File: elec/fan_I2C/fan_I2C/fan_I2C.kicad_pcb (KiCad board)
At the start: 2 copper layers, 83 x 160 mm, 59 parts, among them J101 DB25_Female_MountingHoles, J102 DB9_Female_MountingHoles, J201 0.100_2Pin, J202 S04B-XASK-1(LF)(SN), J301 RJ12_6P6C_HORZ, J302 0.100_2Pin, Q201 BSS138, Q202 BSS138, Q301 BSS138, Q302 BSS138, Q303 BSS138, Q304 BSS138, SW101 SW_DIP_x08

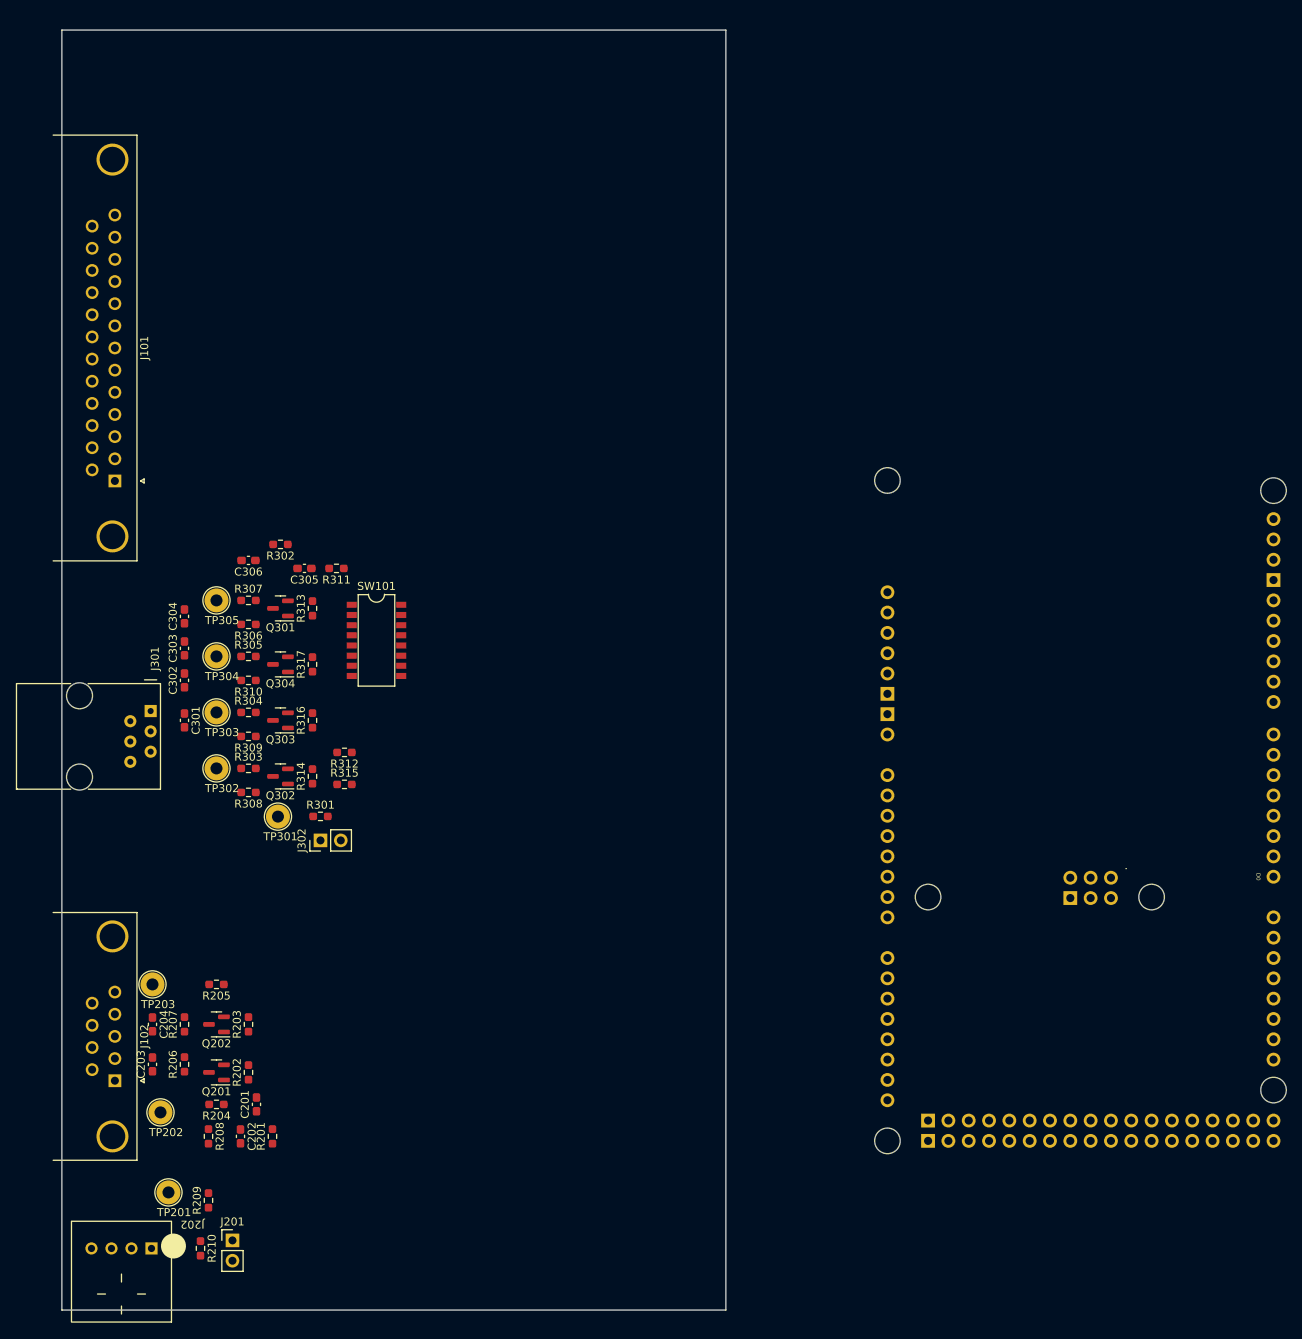
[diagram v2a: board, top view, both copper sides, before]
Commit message: Add connect Due 3V3, 5V and gnd.
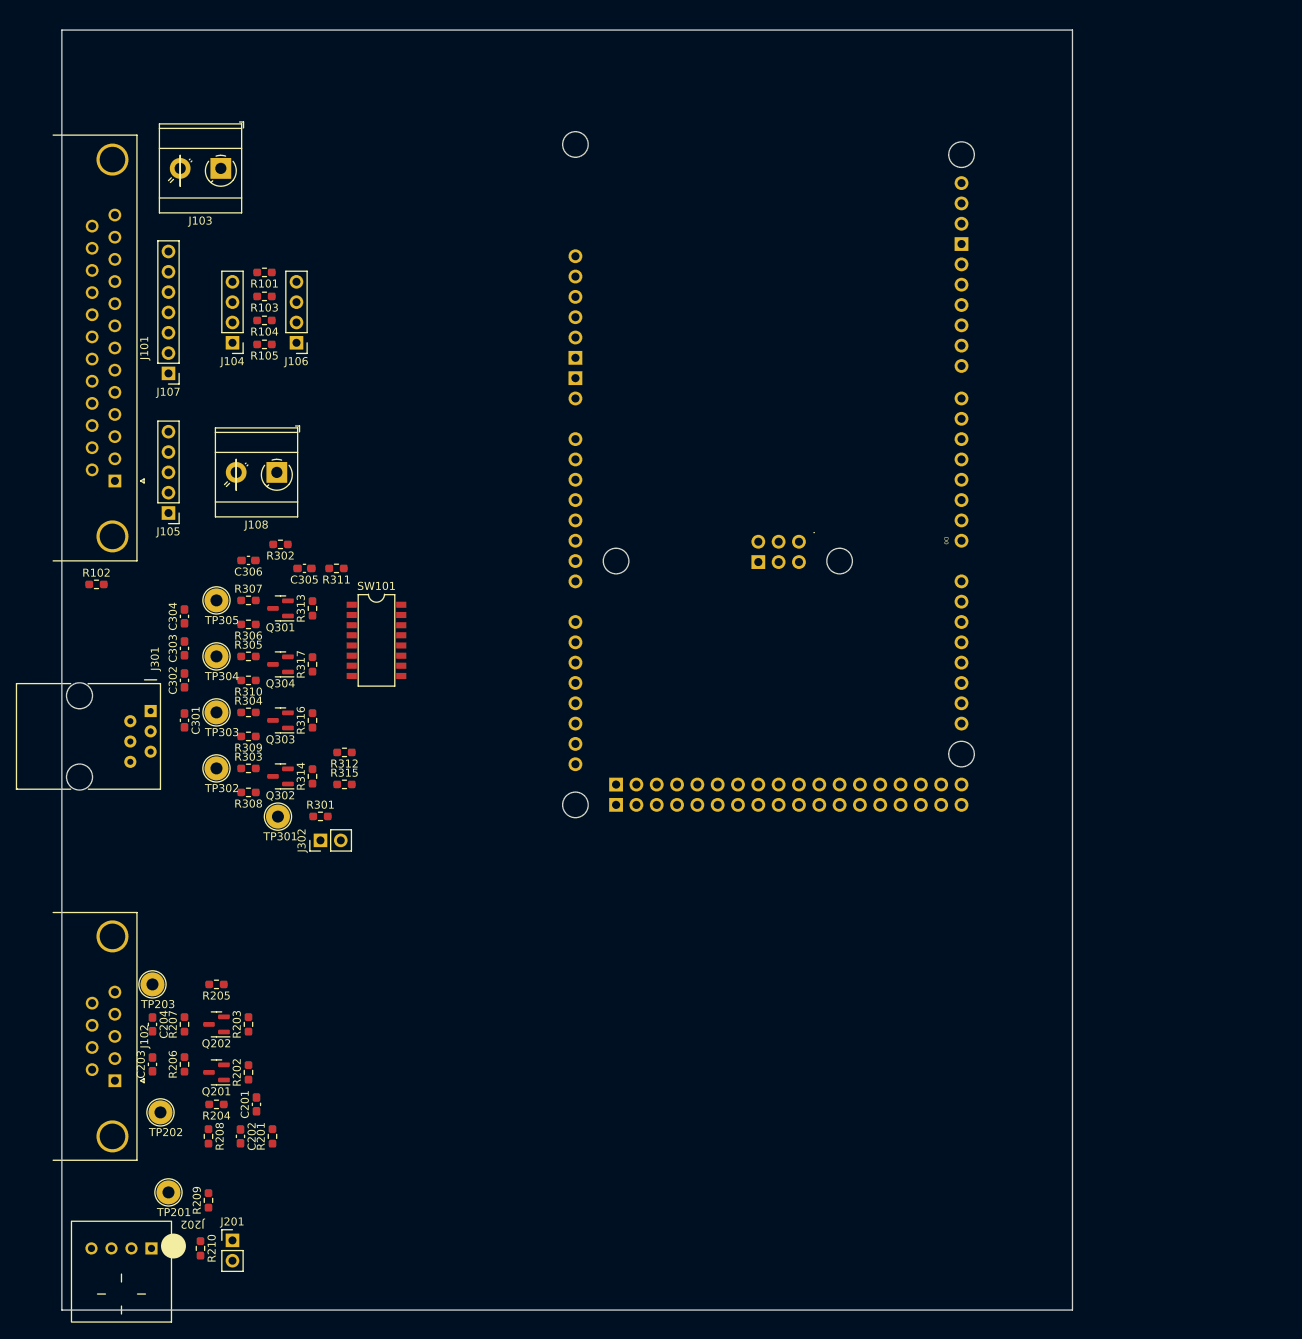
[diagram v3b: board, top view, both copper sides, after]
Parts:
- added J103: Screw_Terminal_01x02, TerminalBlock_MetzConnect:TerminalBlock_MetzConnect_Type073_RT02602HBLU_1x02_P5.08mm_Horizontal, F.Cu at (53.5, 39.0)
- added J104: Conn_01x04, Connector_PinHeader_2.54mm:PinHeader_1x04_P2.54mm_Vertical, F.Cu at (55.0, 60.8)
- added J105: Conn_01x05, Connector_PinHeader_2.54mm:PinHeader_1x05_P2.54mm_Vertical, F.Cu at (47.0, 82.1)
- added J106: Conn_01x04, Connector_PinHeader_2.54mm:PinHeader_1x04_P2.54mm_Vertical, F.Cu at (63.0, 60.8)
- added J107: Conn_01x07, Connector_PinHeader_2.54mm:PinHeader_1x07_P2.54mm_Vertical, F.Cu at (47.0, 64.6)
- added J108: Screw_Terminal_01x02, TerminalBlock_MetzConnect:TerminalBlock_MetzConnect_Type073_RT02602HBLU_1x02_P5.08mm_Horizontal, F.Cu at (60.5, 77.0)
- added R101: 540R, Resistor_SMD:R_0603_1608Metric_Pad0.98x0.95mm_HandSolder, F.Cu at (59.0, 52.0)
- added R102: DNI, Resistor_SMD:R_0603_1608Metric_Pad0.98x0.95mm_HandSolder, F.Cu at (38.0, 91.0)
- added R103: 540R, Resistor_SMD:R_0603_1608Metric_Pad0.98x0.95mm_HandSolder, F.Cu at (59.0, 55.0)
- added R104: 540R, Resistor_SMD:R_0603_1608Metric_Pad0.98x0.95mm_HandSolder, F.Cu at (59.0, 58.0)
- added R105: 540R, Resistor_SMD:R_0603_1608Metric_Pad0.98x0.95mm_HandSolder, F.Cu at (59.0, 61.0)
- moved XA101 57.3 mm to (95.3, 22.0)
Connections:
- J101 pad 1: unconnected-(J101-Pad1) -> Net-(J101-Pad1)
- J101 pad 10: unconnected-(J101-Pad10) -> Net-(J101-Pad10)
- J101 pad 11: unconnected-(J101-Pad11) -> Net-(J101-Pad10)
- J101 pad 12: unconnected-(J101-Pad12) -> Net-(J101-Pad10)
- J101 pad 13: unconnected-(J101-Pad13) -> Net-(J101-Pad13)
- J101 pad 14: GND -> Net-(J101-Pad14)
- J101 pad 15: unconnected-(J101-Pad15) -> Net-(J101-Pad14)
- J101 pad 16: unconnected-(J101-Pad16) -> Net-(J101-Pad14)
- J101 pad 17: unconnected-(J101-Pad17) -> Net-(J101-Pad14)
- J101 pad 18: unconnected-(J101-Pad18) -> Net-(J101-Pad18)
- J101 pad 19: unconnected-(J101-Pad19) -> Net-(J101-Pad19)
- J101 pad 2: unconnected-(J101-Pad2) -> Net-(J101-Pad2)
- J101 pad 20: unconnected-(J101-Pad20) -> Net-(J101-Pad20)
- J101 pad 21: unconnected-(J101-Pad21) -> Net-(J101-Pad21)
- J101 pad 22: unconnected-(J101-Pad22) -> Net-(J101-Pad22)
- J101 pad 23: GND -> Net-(J101-Pad23)
- J101 pad 24: GND -> Net-(J101-Pad24)
- J101 pad 25: GND -> Net-(J101-Pad25)
- J101 pad 3: unconnected-(J101-Pad3) -> Net-(J101-Pad3)
- J101 pad 4: unconnected-(J101-Pad4) -> Net-(J101-Pad4)
- J101 pad 5: unconnected-(J101-Pad5) -> Net-(J101-Pad5)
- J101 pad 6: unconnected-(J101-Pad6) -> Net-(J101-Pad6)
- J101 pad 7: unconnected-(J101-Pad7) -> Net-(J101-Pad7)
- J101 pad 8: unconnected-(J101-Pad8) -> Net-(J101-Pad8)
- J101 pad 9: unconnected-(J101-Pad9) -> Net-(J101-Pad10)
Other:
- board size 83 x 160 mm -> 126.3 x 160 mm

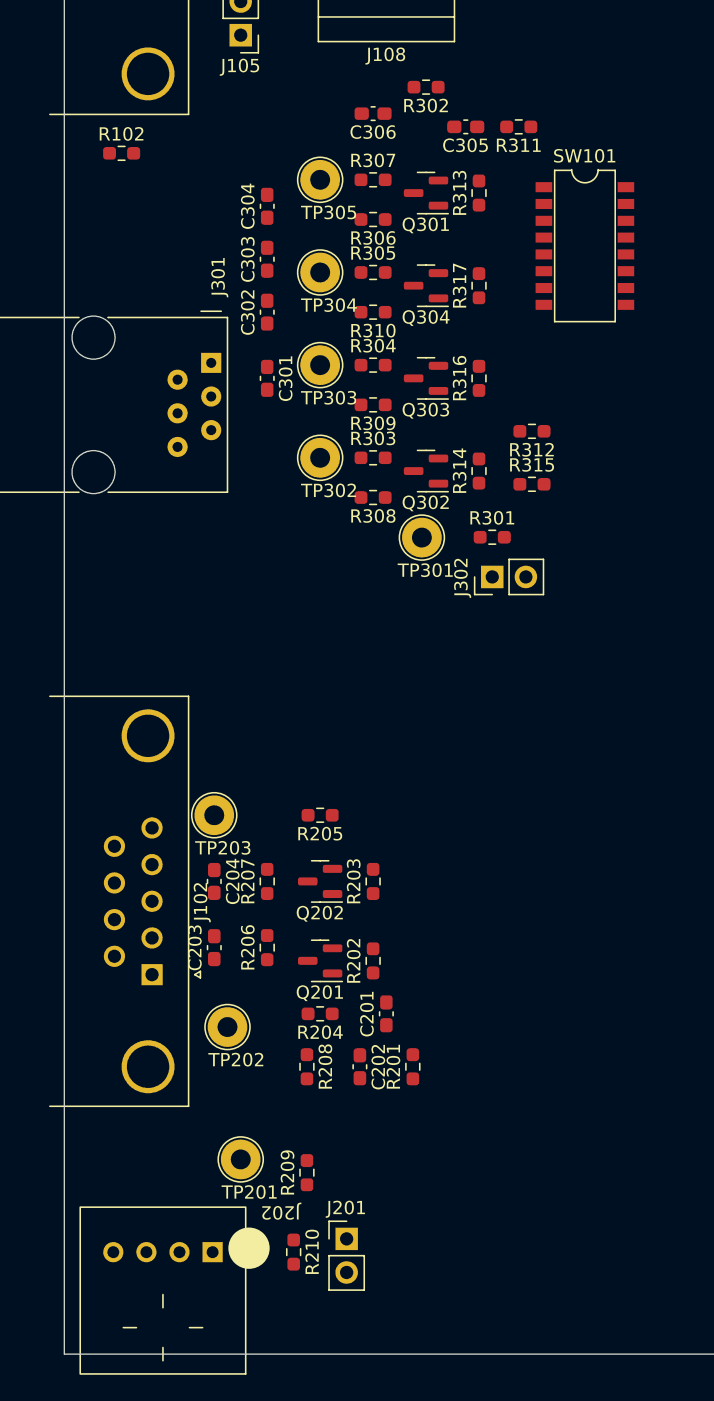
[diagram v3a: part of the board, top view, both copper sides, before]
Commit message: Tweek component placement.
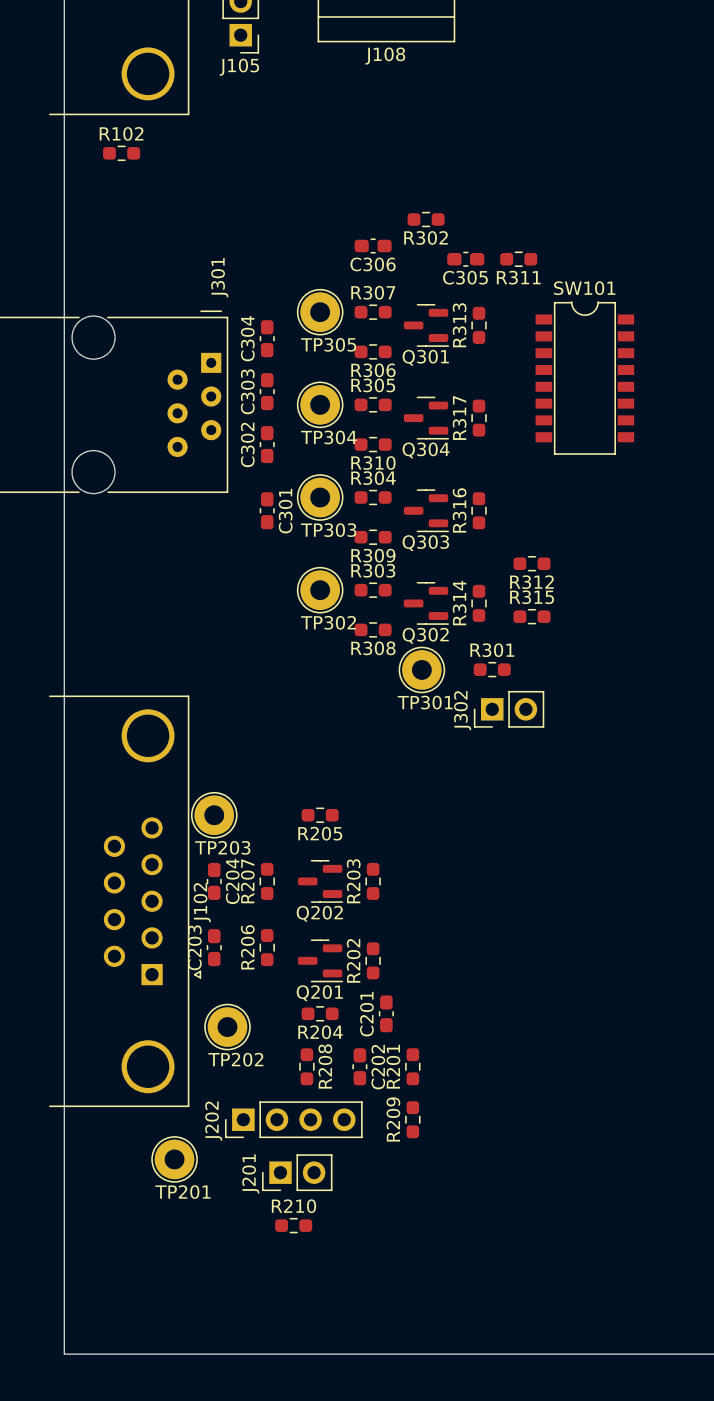
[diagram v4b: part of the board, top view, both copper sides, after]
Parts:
- J202: value S04B-XASK-1(LF)(SN) -> Conn_01x04; footprint PubInv_PCB:S04B-XASK-1(LF)(SN) -> Connector_PinHeader_2.54mm:PinHeader_1x04_P2.54mm_Vertical
- moved J202 20.1 mm to (47.2, 164.0), turned to 90 degrees
- moved TP301 10.0 mm to (60.7, 130.0)
- moved C301 10.0 mm to (49.0, 118.0)
- moved C302 10.0 mm to (49.0, 113.0)
- moved C303 10.0 mm to (49.0, 109.0)
- moved C304 10.0 mm to (49.0, 105.0)
- moved C305 10.0 mm to (64.0, 99.0)
- moved C306 10.0 mm to (57.0, 98.0)
- moved J302 10.0 mm to (66.0, 133.0)
- moved Q301 10.0 mm to (61.0, 104.0)
- moved Q302 10.0 mm to (61.0, 125.0)
- moved Q303 10.0 mm to (61.0, 118.0)
- moved Q304 10.0 mm to (61.0, 111.0)
- moved R301 10.0 mm to (66.0, 130.0)
- moved R302 10.0 mm to (61.0, 96.0)
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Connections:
- XA101 pad 3V3: unconnected-(XA101-Pad3V3) -> +3.3V
- XA101 pad 5V1: unconnected-(XA101-Pad5V1) -> +5V
- XA101 pad 5V3: unconnected-(XA101-Pad5V3) -> +5V
- XA101 pad 5V4: unconnected-(XA101-Pad5V4) -> +5V
- XA101 pad GND1: unconnected-(XA101-PadGND1) -> GND
- XA101 pad GND2: unconnected-(XA101-PadGND2) -> GND
- XA101 pad GND3: unconnected-(XA101-PadGND3) -> GND
- XA101 pad GND5: unconnected-(XA101-PadGND5) -> GND
- XA101 pad GND6: unconnected-(XA101-PadGND6) -> GND

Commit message: Tweeks, perhaps some schematic notes.
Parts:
- added G***: LOGO, PubInv_PCB:Logo_PI_BandW_70percent_10x10, F.Cu at (155.0, 177.0)
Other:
- board text added: "By: Public Invention"
- board text added: "CERN Open Hardware License Version 2 - Strongly Reciprocal"
- board text added: "Model: fan_I2C"
- board text added: "Revision: 1.0 20230330"

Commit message: Add text notes????
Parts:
- added J109: Conn_02x12_Odd_Even, Connector_JST:JST_PHD_B24B-PHDSS_2x12_P2.00mm_Vertical, F.Cu at (118.0, 144.0)
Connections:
- J106 pad 1: Net-(J106-Pad1) -> GND
- J108 pad 1: Net-(J106-Pad1) -> GND
